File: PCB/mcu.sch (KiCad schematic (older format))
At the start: 53 parts, among them J1 DBG, P1 PC, P2 Link, P3 SSD1107, Q1 Q_PNP_BCE, U1 24LC64, U2 TLV62568DBV, U3 USBLC6-2SC6, U4 USBLC6-2SC6, U5 STM32F303CCTx

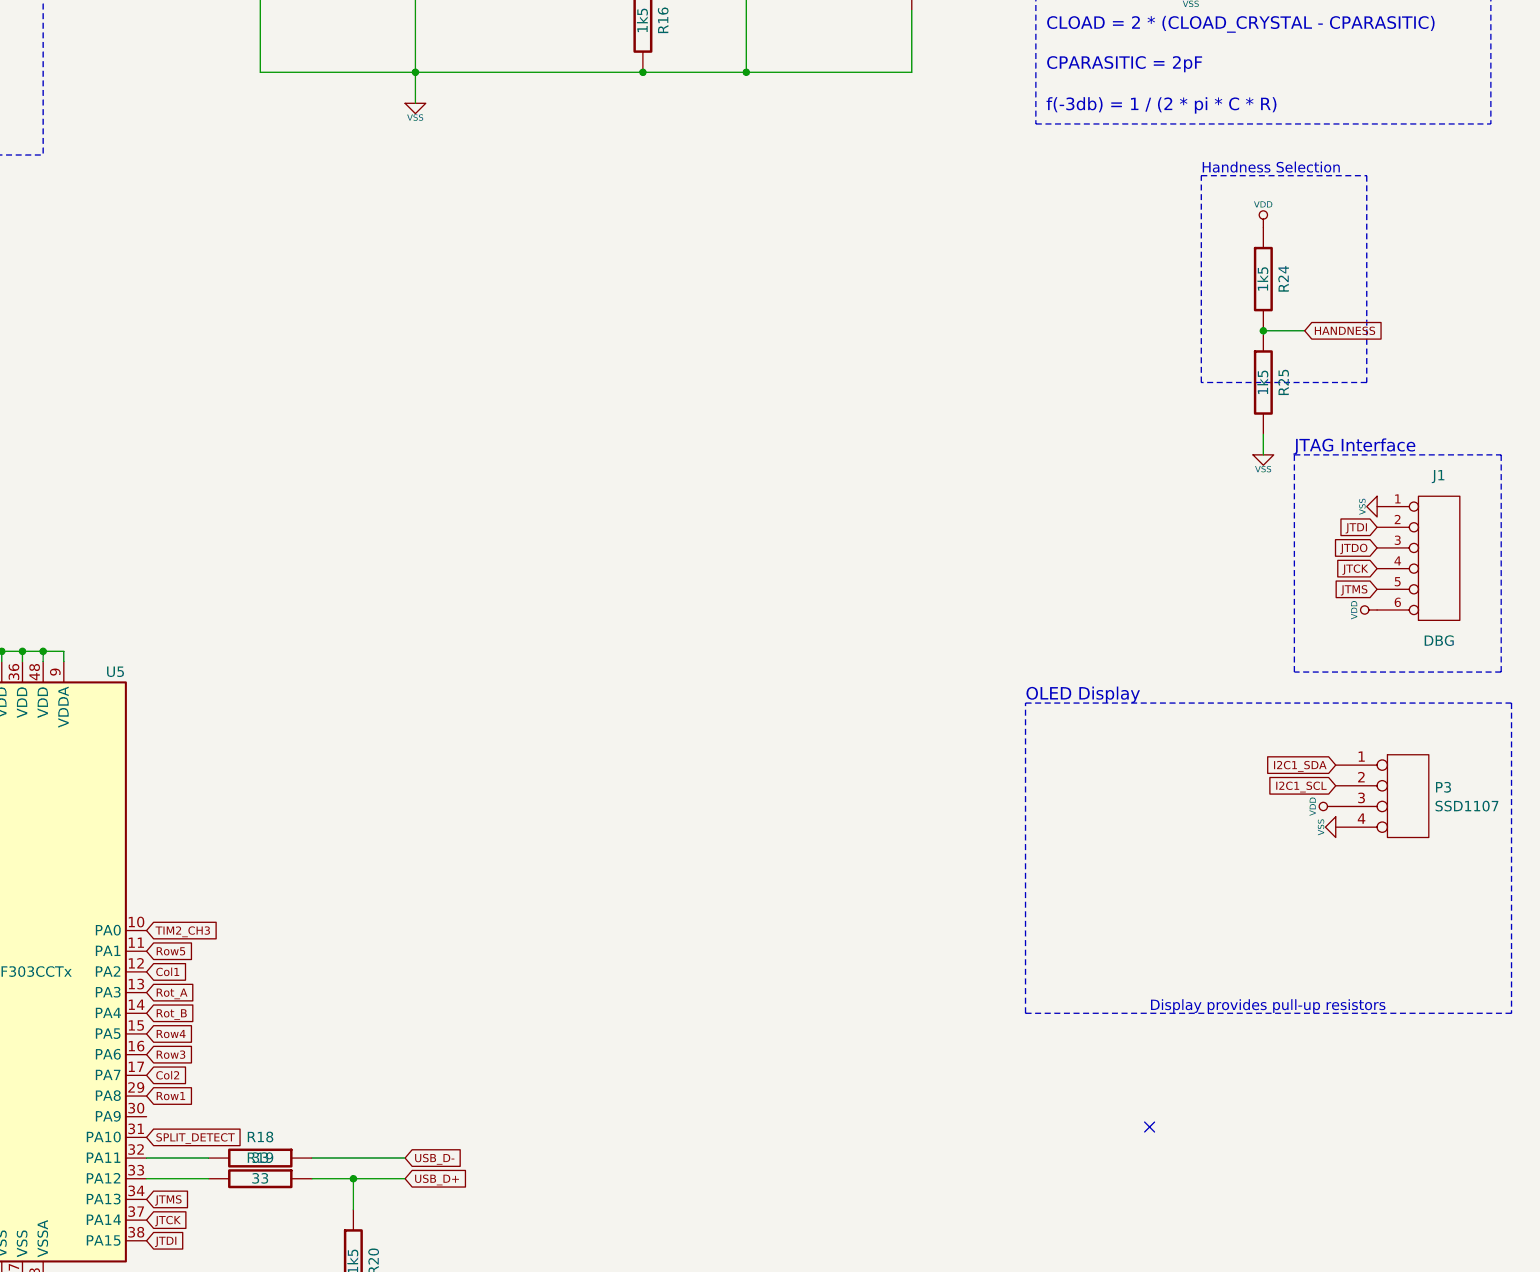
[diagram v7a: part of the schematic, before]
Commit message: Correct RGB DATA
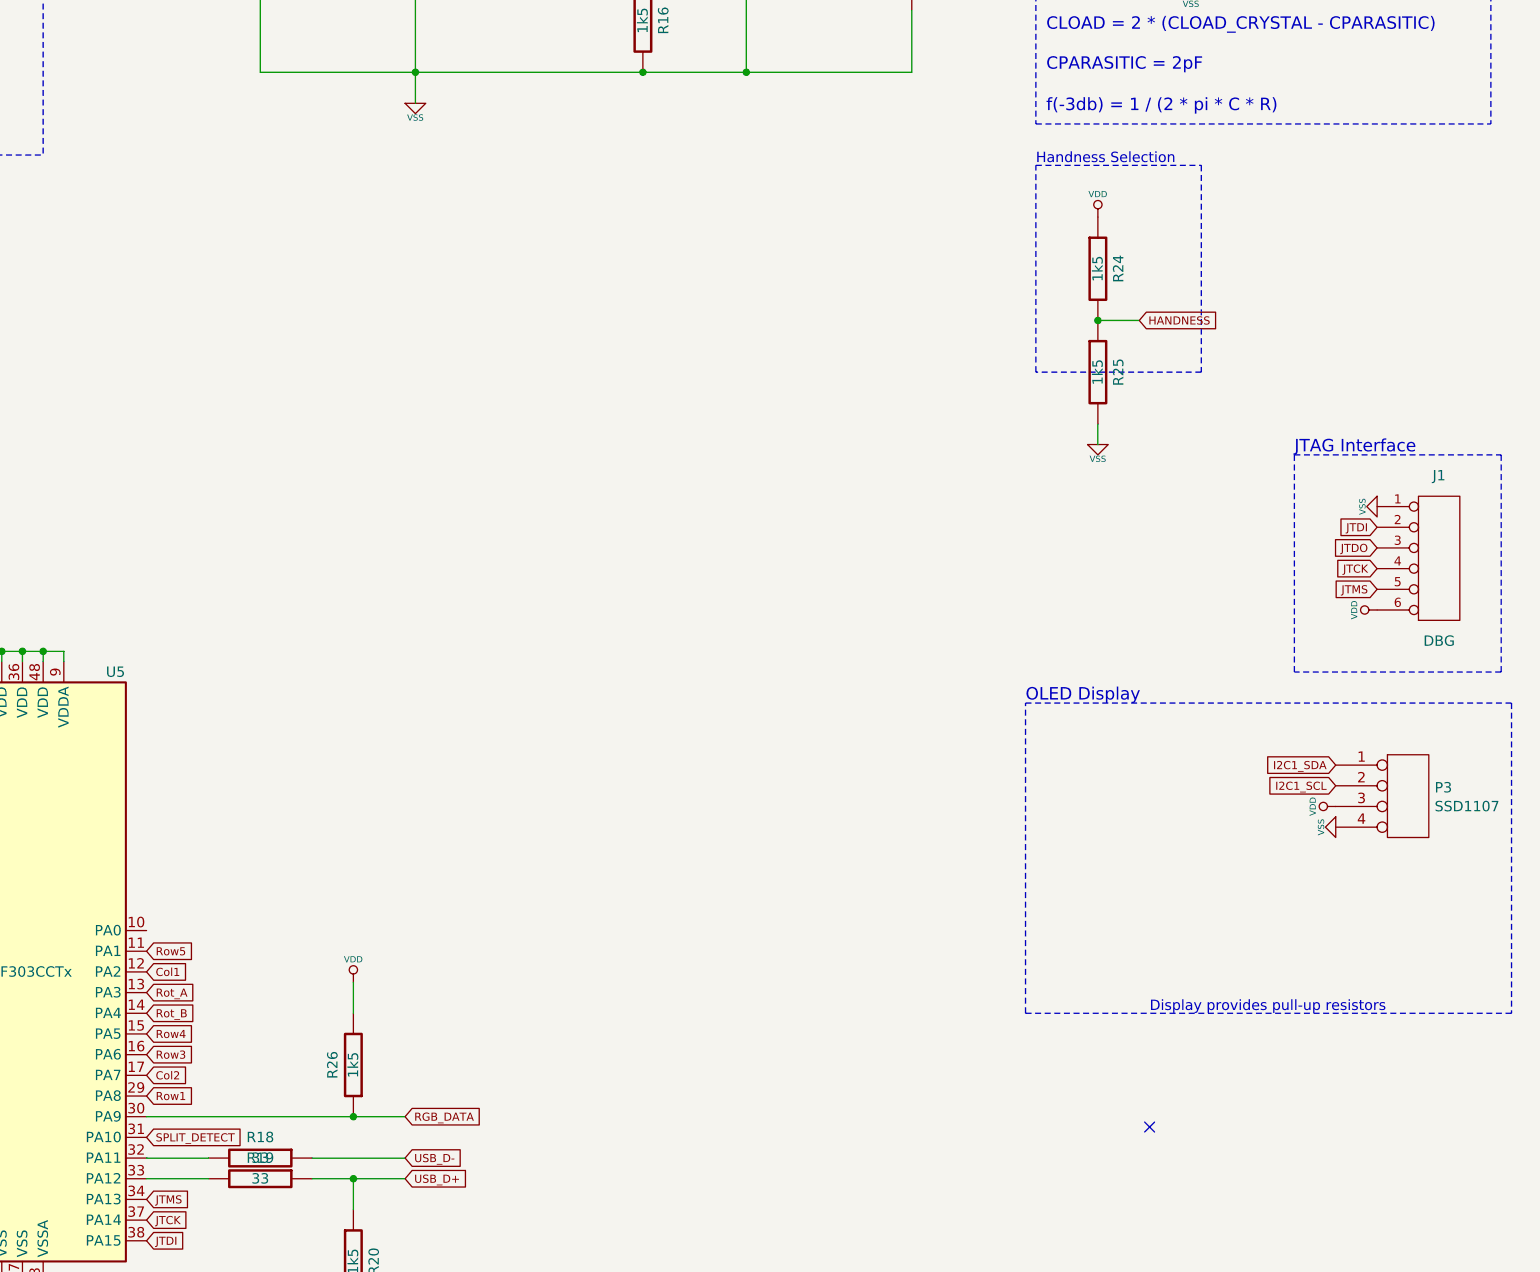
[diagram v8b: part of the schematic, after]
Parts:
- added R26: 1k5, prettylib:SMD-0603, symbol YAEMK:R
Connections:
- net VDD: now also R26.2
- net RGB_DATA: now reaches U5.30 (PA9)
- net RGB_DATA: now also R26.1
- net TIM2_CH3: no longer names the net of U5.10 (PA0)
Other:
- moved on the sheet: R24, R25
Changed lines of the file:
@@
 HANDNESS
 Wire Notes Line
-	15250 3500 14450 3500
-Wire Notes Line
-	14450 3500 14450 2500
-Wire Notes Line
-	14450 2500 15250 2500
-Wire Notes Line
-	15250 2500 15250 3500
-Text Notes 14450 2500 0    50   ~ 0
+	14450 3450 13650 3450
+Wire Notes Line
+	13650 3450 13650 2450
+Wire Notes Line
+	13650 2450 14450 2450
+Wire Notes Line
+	14450 2450 14450 3450
+Text Notes 13650 2450 0    50   ~ 0
 Handness Selection
 Wire Notes Line
@@
 	13050 2000 12250 2000
 Connection ~ 12250 2000
-Text GLabel 9350 6150 2    39   Input ~ 0
-TIM2_CH3
+Text GLabel 10600 7050 2    39   Input ~ 0
+RGB_DATA
 $Comp
 L Device:D_Schottky D77
@@
 L YAEMK:R R24
 U 1 1 5FBBBB46
-P 14750 3000
-F 0 "R24" V 14850 3000 50  0000 C CNN
-F 1 "1k5" V 14750 3000 50  0000 C CNN
-F 2 "prettylib:SMD-0603" V 14650 3000 60  0001 C CNN
-F 3 "" H 14750 3000 60  0001 C CNN
-	1    14750 3000
+P 13950 2950
+F 0 "R24" V 14050 2950 50  0000 C CNN
+F 1 "1k5" V 13950 2950 50  0000 C CNN
+F 2 "prettylib:SMD-0603" V 13850 2950 60  0001 C CNN
+F 3 "" H 13950 2950 60  0001 C CNN
+	1    13950 2950
 	1    0    0    -1
 $EndComp
@@
 L YAEMK:R R25
 U 1 1 5FBBBB50
-P 14750 3500
-F 0 "R25" V 14850 3500 50  0000 C CNN
-F 1 "1k5" V 14750 3500 50  0000 C CNN
-F 2 "prettylib:SMD-0603" V 14650 3500 60  0001 C CNN
-F 3 "" H 14750 3500 60  0001 C CNN
-	1    14750 3500
+P 13950 3450
+F 0 "R25" V 14050 3450 50  0000 C CNN
+F 1 "1k5" V 13950 3450 50  0000 C CNN
+F 2 "prettylib:SMD-0603" V 13850 3450 60  0001 C CNN
+F 3 "" H 13950 3450 60  0001 C CNN
+	1    13950 3450
 	1    0    0    -1
 $EndComp
@@
 L YAEMK:VSS #PWR0111
 U 1 1 5FBBBB5A
-P 14750 3850
-F 0 "#PWR0111" H 14750 3850 30  0001 C CNN
-F 1 "VSS" H 14750 3780 30  0000 C CNN
-F 2 "" H 14750 3850 60  0000 C CNN
-F 3 "" H 14750 3850 60  0000 C CNN
-	1    14750 3850
-	1    0    0    -1
-$EndComp
-Wire Wire Line
-	14750 3750 14750 3850
-Wire Wire Line
-	14950 3250 14750 3250
-Connection ~ 14750 3250
+P 13950 3800
+F 0 "#PWR0111" H 13950 3800 30  0001 C CNN
+F 1 "VSS" H 13950 3730 30  0000 C CNN
+F 2 "" H 13950 3800 60  0000 C CNN
+F 3 "" H 13950 3800 60  0000 C CNN
+	1    13950 3800
+	1    0    0    -1
+$EndComp
+Wire Wire Line
+	13950 3700 13950 3800
+Wire Wire Line
+	14150 3200 13950 3200
+Connection ~ 13950 3200
 $Comp
 L YAEMK:VDD #PWR0112
 U 1 1 5FBC8873
-P 14750 2750
-F 0 "#PWR0112" H 14750 2850 30  0001 C CNN
-F 1 "VDD" H 14750 2860 30  0000 C CNN
-F 2 "" H 14750 2750 60  0000 C CNN
-F 3 "" H 14750 2750 60  0000 C CNN
-	1    14750 2750
-	1    0    0    -1
-$EndComp
-Text GLabel 14950 3250 2    39   Input ~ 0
+P 13950 2700
+F 0 "#PWR0112" H 13950 2800 30  0001 C CNN
+F 1 "VDD" H 13950 2810 30  0000 C CNN
+F 2 "" H 13950 2700 60  0000 C CNN
+F 3 "" H 13950 2700 60  0000 C CNN
+	1    13950 2700
+	1    0    0    -1
+$EndComp
+Text GLabel 14150 3200 2    39   Input ~ 0
 HANDNESS
 $Comp
@@
 	1    0    0    -1
 $EndComp
+Wire Wire Line
+	10350 6550 10350 6400
+$Comp
+L YAEMK:R R26
+U 1 1 5FBB4BC3
+P 10350 6800
+F 0 "R26" V 10450 6800 50  0000 C CNN
+F 1 "1k5" V 10350 6800 50  0000 C CNN
+F 2 "prettylib:SMD-0603" V 10250 6800 60  0001 C CNN
+F 3 "" H 10350 6800 60  0001 C CNN
+	1    10350 6800
+	-1   0    0    1
+$EndComp
+$Comp
+L YAEMK:VDD #PWR0113
+U 1 1 5FBB4BCD
+P 10350 6400
+F 0 "#PWR0113" H 10350 6500 30  0001 C CNN
+F 1 "VDD" H 10350 6510 30  0000 C CNN
+F 2 "" H 10350 6400 60  0000 C CNN
+F 3 "" H 10350 6400 60  0000 C CNN
+	1    10350 6400
+	1    0    0    -1
+$EndComp
+Wire Wire Line
+	10600 7050 10350 7050
+Connection ~ 10350 7050
+Wire Wire Line
+	10350 7050 9350 7050
 $EndSCHEMATC
